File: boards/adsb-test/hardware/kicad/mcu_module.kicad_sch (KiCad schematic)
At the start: 26 parts, among them J601 C5 JTAG (DNP), SW601 BOOT, SW602 RESET, U601 WT01P4C5-S1-N16R32, Y601 32.768kHz

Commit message: Release v0.24.0: OSPTEK ESP32-P4C5 Core module replaces WT01P4C5-S1
Co-Authored-By: Claude Opus 5.5 <noreply@anthropic.com>
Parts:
- removed J601: C5 JTAG (DNP), Connector_PinHeader_1.27mm:PinHeader_2x05_P1.27mm_Vertical_SMD, symbol Connector:Conn_ARM_JTAG_SWD_10
- removed U601: WT01P4C5-S1-N16R32, ADSB_Test:Wireless-Tag_WT01P4C5-S1_HandSolder, symbol ADSB_Test:Wireless-Tag_WT01P4C5-S1
- added C608: 100nF, Capacitor_SMD:C_0805_2012Metric_Pad1.18x1.45mm_HandSolder, symbol Device:C
- added R606: 330R, Resistor_SMD:R_0805_2012Metric_Pad1.20x1.40mm_HandSolder, symbol Device:R
- added R607: 10k, Resistor_SMD:R_0805_2012Metric_Pad1.20x1.40mm_HandSolder, symbol Device:R
- added TP610: P4_GPIO36, TestPoint:TestPoint_Pad_D1.5mm, symbol Connector:TestPoint
- added TP611: C5_PU, TestPoint:TestPoint_Pad_D1.5mm, symbol Connector:TestPoint
- added U601: ESP32-P4C5 Core (OSPTEK), ADSB_Test:OSPTEK_ESP32-P4C5_Core_HandSolder, symbol ADSB_Test:OSPTEK_ESP32-P4C5_Core
- TP601: value C5_IO1 -> C5_IO27
- TP602: value C5_IO6 -> C5_IO25
- TP603: value C5_IO23 -> C5_IO24
- TP604: value C5_IO24 -> C5_IO23
- TP605: value C5_IO25 -> C5_IO6
- TP606: value C5_IO27 -> C5_IO5
- TP607: value P4_GPIO36 -> C5_IO4
- TP608: value P4_GPIO54 -> P4_GPIO12
- TP609: value MCU_PWR_CTRL -> P4_GPIO20
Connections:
- net C5_IO1 is gone; now on net C5_IO27: TP601.1
- net C5_BOOT: now also U601.6 (C5_IO28/BOOT)
- net C5_CON_RX: now also U601.4 (C5_U0RXD)
- net C5_CON_TX: now also U601.5 (C5_U0TXD)
- net C5_EN: now also R606.2
- net C5_IO23: now also TP604.1, U601.11 (C5_IO23); no longer TP603.1
- net C5_IO24: now also TP603.1, U601.10 (C5_IO24); no longer TP604.1
- net C5_IO25: now also TP602.1, U601.9 (C5_IO25); no longer TP605.1
- net C5_IO26: now also U601.8 (C5_IO26)
- net C5_IO27: now also U601.7 (C5_IO27); no longer TP606.1
- net C5_IO6: now also TP605.1, U601.12 (C5_IO6); no longer TP602.1
- net CHG_PD_INT: now also U601.24 (GPIO9)
- net DBG_A: now also U601.25 (GPIO10)
- net DBG_B: now also U601.26 (GPIO11)
- net DSI_CLK_N: now also U601.36 (DSI_CLKN)
- net DSI_CLK_P: now also U601.37 (DSI_CLKP)
- net DSI_D0_N: now also U601.39 (DSI_D0N)
- net DSI_D0_P: now also U601.38 (DSI_D0P)
- net DSI_D1_N: now also U601.35 (DSI_D1N)
- net DSI_D1_P: now also U601.34 (DSI_D1P)
- net ETH_CRS_DV: now also U601.55 (GPIO28)
- net ETH_MDC: now also U601.58 (GPIO31)
- net ETH_MDIO: now also U601.80 (GPIO52)
- net ETH_PHY_RST: now also U601.79 (GPIO51)
- net ETH_REF_CLK: now also U601.78 (GPIO50)
- net ETH_RXD0: now also U601.56 (GPIO29)
- net ETH_RXD1: now also U601.57 (GPIO30)
- net ETH_TXD0: now also U601.61 (GPIO34)
- net ETH_TXD1_BOOT: now also U601.62 (GPIO35/BOOT)
- net ETH_TX_EN: now also U601.77 (GPIO49)
- net EXP_INT: now also U601.81 (GPIO53)
- net GND: now also C608.2, U601.1 (GND), U601.15 (GND), U601.3 (GND), U601.33 (GND), U601.40 (GND), U601.47 (GND), U601.52 (GND), U601.83 (GND)
- net GPS_PPS: now also U601.19 (GPIO4)
- net GPS_TX: now also U601.18 (GPIO3)
- net I2C_SCL: now also U601.23 (GPIO8)
- net I2C_SDA: now also U601.22 (GPIO7)
- net LCD_BL_PWM: now also U601.59 (GPIO32)
- net LCD_RST: now also U601.60 (GPIO33)
- net M1421_SUTX: now also U601.75 (GPIO47)
- net P4_CON_RX: now also U601.65 (GPIO38/U0RXD)
- net P4_CON_TX: now also U601.64 (GPIO37/U0TXD)
- net P4_EN: now also R607.2, U601.87 (CHIP_PU)
- net P4_GPIO36: now also TP610.1, U601.63 (GPIO36); no longer TP607.1
- net P4_GPS_TX: now also U601.17 (GPIO2)
- net P4_M1421_SYNC: now also U601.76 (GPIO48)
- net P4_M1421_TX: now also U601.74 (GPIO46)
- net P4_USER_RX: now also U601.31 (GPIO22)
- net P4_USER_TX: now also U601.30 (GPIO21)
- net P4_USJ_DM: now also U601.50 (GPIO24/USB_JTAG_N)
- net P4_USJ_DP: now also U601.51 (GPIO25/USB_JTAG_P)
- net PM_ALERT: now also U601.20 (GPIO5)
- net RTC_INT: now also U601.28 (GPIO13)
- net SD_CLK: now also U601.71 (GPIO43)
- net SD_CMD: now also U601.72 (GPIO44)
- net SD_D0: now also U601.67 (GPIO39)
- net SD_D1: now also U601.68 (GPIO40)
- net SD_D2: now also U601.69 (GPIO41)
- net SD_D3: now also U601.70 (GPIO42)
- net SD_PWR_EN: now also U601.73 (GPIO45)
- net SD_VIO: now also U601.66 (ESP_LDO_VO4)
- net TOUCH_INT: now also U601.53 (GPIO26)
- net TOUCH_RST: now also U601.32 (GPIO23)
- net USBA_FAULT: now also U601.54 (GPIO27)
- net USB_HS_DM: now also U601.48 (USB_DM)
- net USB_HS_DP: now also U601.49 (USB_DP)
- net XTAL32_N: now also U601.88 (GPIO0/XTAL_32K_N)
- net XTAL32_P: now also U601.16 (GPIO1/XTAL_32K_P)
- net 5V_MCU renamed 3V3_MCU
- net 3V3_MCU: now also R607.1, U601.85 (ESP_3V3), U601.86 (ESP_3V3)
- net MCU_PWR_CTRL renamed P4_GPIO20
- net P4_GPIO20: now also U601.29 (GPIO20)
- net P4_GPIO54 renamed P4_GPIO12
- net P4_GPIO12: now also U601.27 (GPIO12)
- new net C5_IO4: TP607.1, U601.14 (C5_IO4)
- new net C5_IO5: TP606.1, U601.13 (C5_IO5)
- new net C5_PU: R606.1, TP611.1, U601.82 (GPIO54/C5_CHIP_PU)
- new net VBACKUP: C608.1, U601.84 (RTC_VBAT)
- no-connect marks 10 -> 8
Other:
- note added: "MCU MODULE: OSPTEK ESP32-P4C5 Core (ESP32-P4 rev v3.x + ESP32-C5HF4, 16 MB flash, 32 MB PSRAM). Inside the module: SDIO on P4 GPIO14-19, C5 CHIP_PU = P4 GPIO54 (pad 82), C5 GPIO2 = P4 GPIO6 (pad 21, NC here) - the same wiring as the Waveshare reference board. Pins: bsp/include/bsp/board_pins.h. 3.3 V supply (3V3_MCU, shunt RS404 / PM2 CH2). RTC_VBAT from VBACKUP (always on): P4 RTC keeps time whe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"
- note removed: "MCU MODULE: Wireless-Tag WT01P4C5-S1 (ESP32-P4 + ESP32-C5, SDIO inside: P4 GPIO14-19, C5 CHIP_PU = P4 GPIO13, C5 GPIO0 = P4 GPIO12). Pins: bsp/include/bsp/board_pins.h. 5 V supply only (5V_MCU, shunt RS404 / PM2 CH2); PWR_CTRL left to its internal pull-up (TP). No P4 VBAT on this module: wall-clock time is kept by the DS3231M (RTC sheet). Wi-Fi: IPEX on the module -> U.FL pigtail -> antenna at th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"

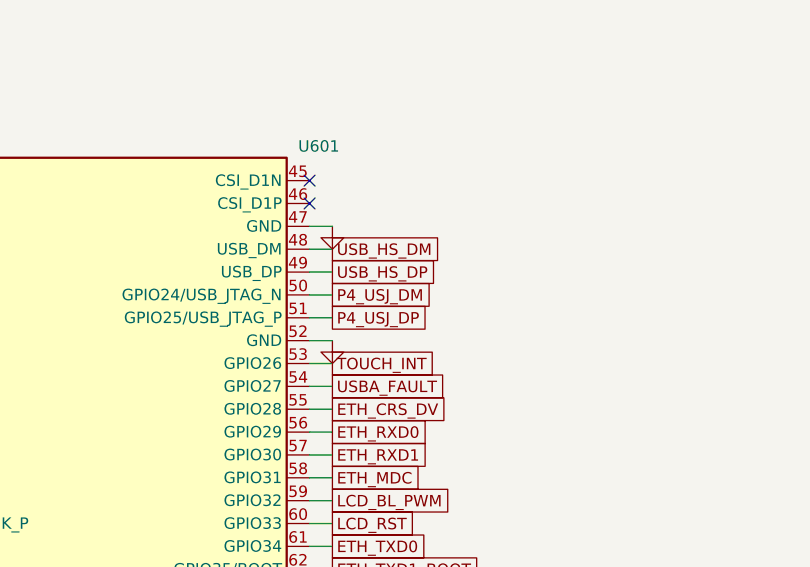
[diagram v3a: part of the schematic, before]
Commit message: ADSB_Test: net classes + diff-pair rules, USB pairs renamed _D_P/_D_N, U201 VSYS drawn at the bottom
Co-Authored-By: Claude Opus 5.5 <noreply@anthropic.com>
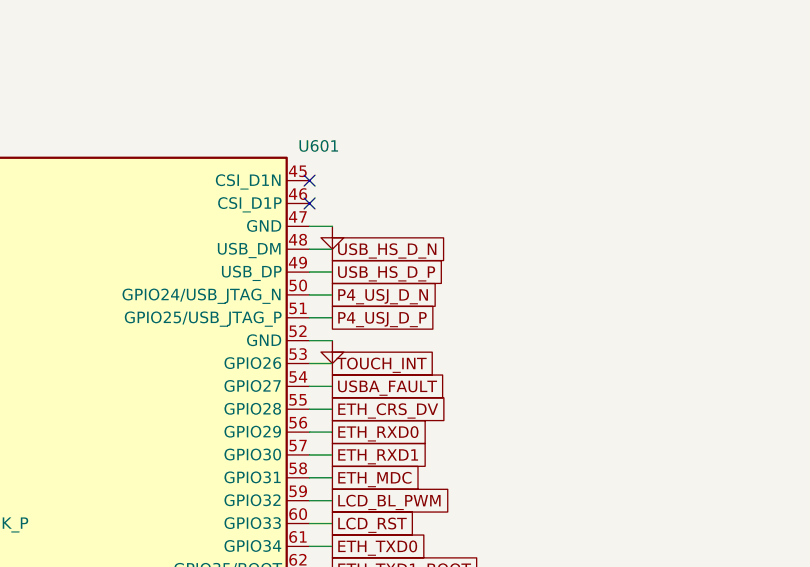
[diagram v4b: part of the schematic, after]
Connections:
- net P4_USJ_DM renamed P4_USJ_D_N
- net P4_USJ_DP renamed P4_USJ_D_P
- net USB_HS_DM renamed USB_HS_D_N
- net USB_HS_DP renamed USB_HS_D_P

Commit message: ADSB_Test: SLEEP/WAKE button on GPIO12 with BSP deep-sleep support
SW603 right-angle tactile on the digital edge next to POWER, 10k pull-up on
3V3_MCU, 470R + 100nF. bsp_sleep() turns the expander rails off, holds the C5
in reset and deep-sleeps the P4 with ext1 wake on the button (and optionally
the DS3231M alarm). [sleep] test, BOM line, docs, PCB regenerated.

Co-Authored-By: Claude Opus 5.5 <noreply@anthropic.com>
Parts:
- added C609: 100nF, Capacitor_SMD:C_0805_2012Metric_Pad1.18x1.45mm_HandSolder, symbol Device:C
- added R608: 10k, Resistor_SMD:R_0805_2012Metric_Pad1.20x1.40mm_HandSolder, symbol Device:R
- added R609: 470R, Resistor_SMD:R_0805_2012Metric_Pad1.20x1.40mm_HandSolder, symbol Device:R
- added SW603: SLEEP/WAKE, Button_Switch_THT:SW_Tactile_SPST_Angled_PTS645Vx31-2LFS, symbol Switch:SW_Push
- TP608: value P4_GPIO12 -> SLEEP_WAKE
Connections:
- net 3V3_MCU: now also R608.1
- net GND: now also C609.2, SW603.2
- net P4_GPIO12 renamed SLEEP_WAKE
- net SLEEP_WAKE: now also C609.1, R609.2
- new net SLEEP_BTN: R608.2, R609.1, SW603.1

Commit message: ADSB_Test: Kelvin shunt footprint, Wi-Fi RP-SMA on the top edge, PCB parity 0
- Shunts RS201-RS409: 4-pad R_Shunt_1206_Kelvin_HandSolder (net-tied sense
  pads) replaces the 2-pad 1206, which put the sense net on the load pad.
- Wi-Fi: module IPEX -> U.FL jumper -> J601 -> J602 RP-SMA on the top long
  edge, away from the 1090/978 and GNSS SMAs. BOM, datasheets, docs.
- gen_pcb: symbol fields and BOM flags copied to footprints, unconnected
  net names escaped; top-edge placement.

Co-Authored-By: Claude Opus 5.5 <noreply@anthropic.com>
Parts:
- added J601: U.FL Wi-Fi (from module IPEX), Connector_Coaxial:U.FL_Hirose_U.FL-R-SMT-1_Vertical, symbol Connector:Conn_Coaxial
- added J602: RP-SMA Wi-Fi 2.4/5 GHz, Connector_Coaxial:SMA_Molex_73251-1153_EdgeMount_Horizontal, symbol Connector:Conn_Coaxial
- U601: Antenna IPEX (U.FL) on the module: pigtail to a 2.4/5 GHz antenna -> IPEX (U.FL) on the module: jumper to J601 -> J602 RP-SMA
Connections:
- net GND: now also J601.2 (Ext), J602.2 (Ext)
- new net WIFI_ANT: J601.1 (In), J602.1 (In)

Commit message: ADSB_Test: J602 footprint from the Molex 73251-3152 drawing, floorplan PNG refreshed
KiCad's 73251-1153 footprint did not match the 73251-3152 pad layout.
New SMA_Molex_73251-3152_RP_EdgeMount from SD-73251-315 (pads both sides,
plated holes, PCB Edge marker), pads 0.25 mm in from the edge with a 0.2 mm
edge-clearance rule for J602. Sales drawing registered; floorplan.png
regenerated to match the SVG.

Co-Authored-By: Claude Opus 5.5 <noreply@anthropic.com>
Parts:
- J602: footprint Connector_Coaxial:SMA_Molex_73251-1153_EdgeMount_Horizontal -> ADSB_Test:SMA_Molex_73251-3152_RP_EdgeMount; Check Molex 0732513152 (RP, bulkhead nut): confirm pads vs PS-896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 -> (none); MPN (none) -> Molex 0732513152 (RP-SMA, jam nut); footprint from SD-73251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
